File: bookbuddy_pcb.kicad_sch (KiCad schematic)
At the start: 0 parts

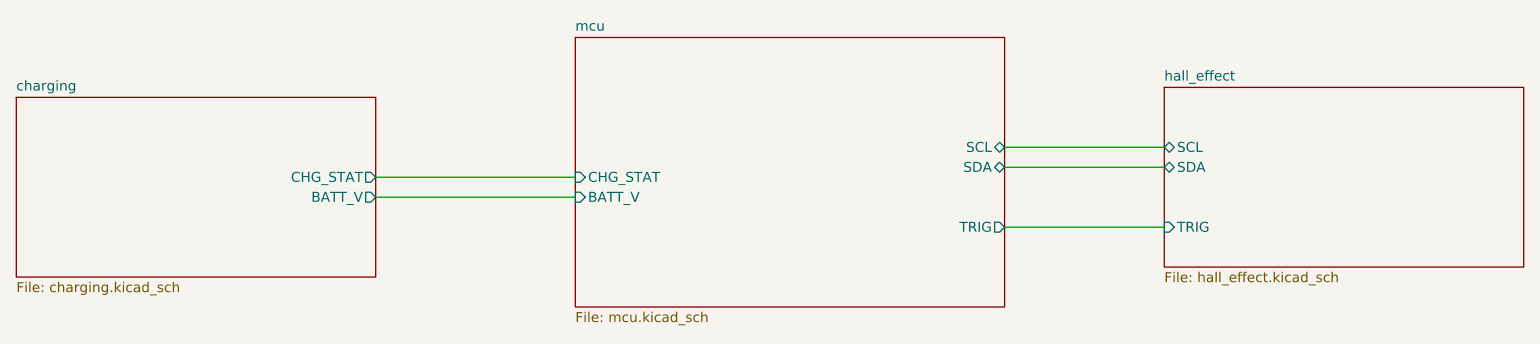
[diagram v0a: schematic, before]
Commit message: Made changes up to diode logic
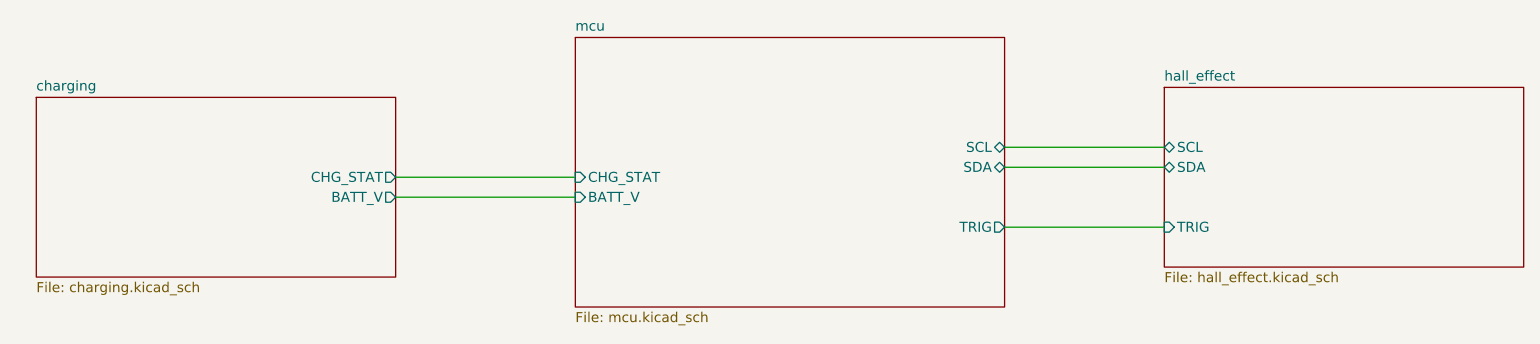
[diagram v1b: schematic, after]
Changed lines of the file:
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@@
 	(wire
 		(pts
-			(xy 97.79 97.79) (xy 123.19 97.79)
-		)
-		(stroke
-			(width 0)
-			(type default)
-		)
-	)
-	(wire
-		(pts
-			(xy 97.79 95.25) (xy 123.19 95.25)
+			(xy 100.33 97.79) (xy 123.19 97.79)
+		)
+		(stroke
+			(width 0)
+			(type default)
+		)
+	)
+	(wire
+		(pts
+			(xy 100.33 95.25) (xy 123.19 95.25)
 		)
 		(stroke
@@
 	)
 	(sheet
-		(at 52.07 85.09)
+		(at 54.61 85.09)
 		(size 45.72 22.86)
 		(fields_autoplaced yes)
@@
 		)
 		(property "Sheetname" "charging"
-			(at 52.07 84.3784 0)
+			(at 54.61 84.3784 0)
 			(effects
 				(font
@@
 		)
 		(property "Sheetfile" "charging.kicad_sch"
-			(at 52.07 108.5346 0)
+			(at 54.61 108.5346 0)
 			(effects
 				(font
@@
 		)
 		(pin "CHG_STAT" output
-			(at 97.79 95.25 0)
+			(at 100.33 95.25 0)
 			(effects
 				(font
@@
 		)
 		(pin "BATT_V" output
-			(at 97.79 97.79 0)
-			(effects
-				(font
+			(at 100.33 97.79 0)
+			(effects
+				(font
